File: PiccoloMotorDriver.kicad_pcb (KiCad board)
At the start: 6 copper layers, 60 x 60 mm, 114 parts, among them J10 AUX2, J11 C189893, J12 C265111, J2 01x03_MotorTerminal, J3 C189893, J4 C225127, J5 Screw_Terminal_01x02_POWER, J6 Connector, USB-TYPE-C-16P, J7 C225127, J8 AUX0, J9 AUX1, Q1 NE006NG, Q2 NE006NG, Q3 NE006NG, Q4 NE006NG, Q5 NE006NG, Q6 NE006NG, U1 SP485EEN, U2 XC6210B332MR, U3 XL1509, U4 TJA1050T/CM,118, U5 AS5047D, U6 USBLC6-2SC6, X2 X322516MLB4SI

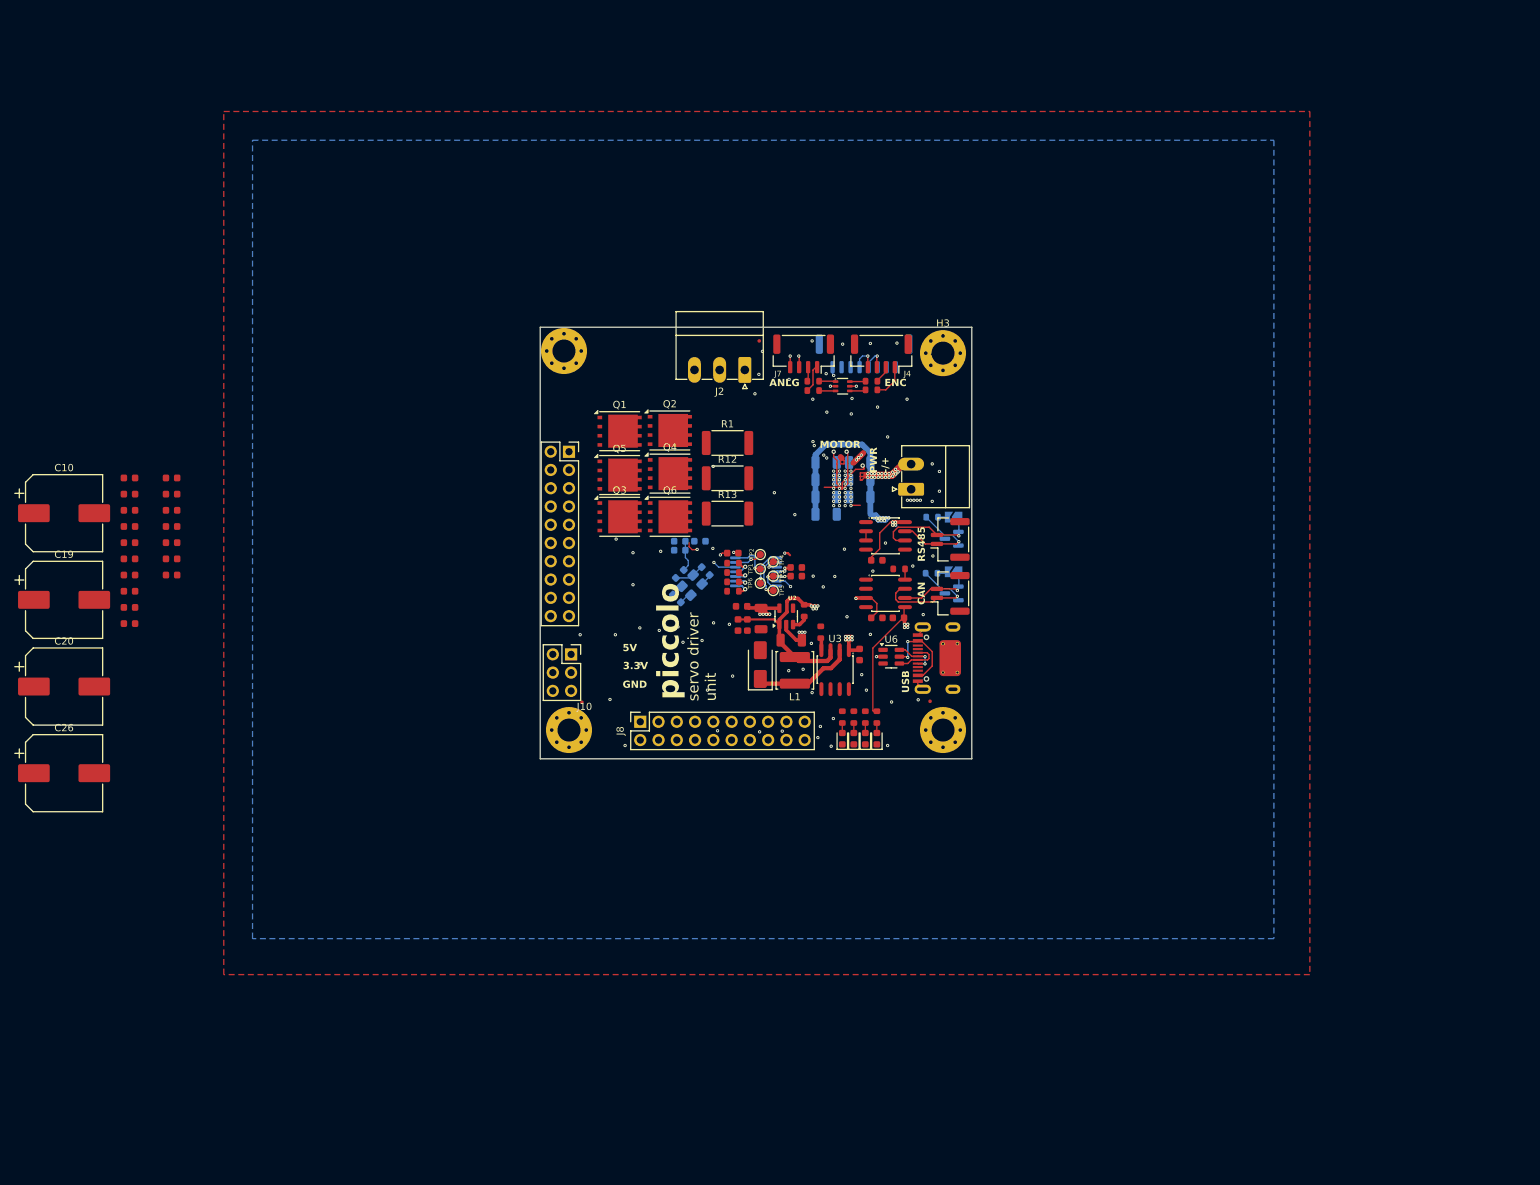
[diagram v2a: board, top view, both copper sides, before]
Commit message: Circular pcb edge cut
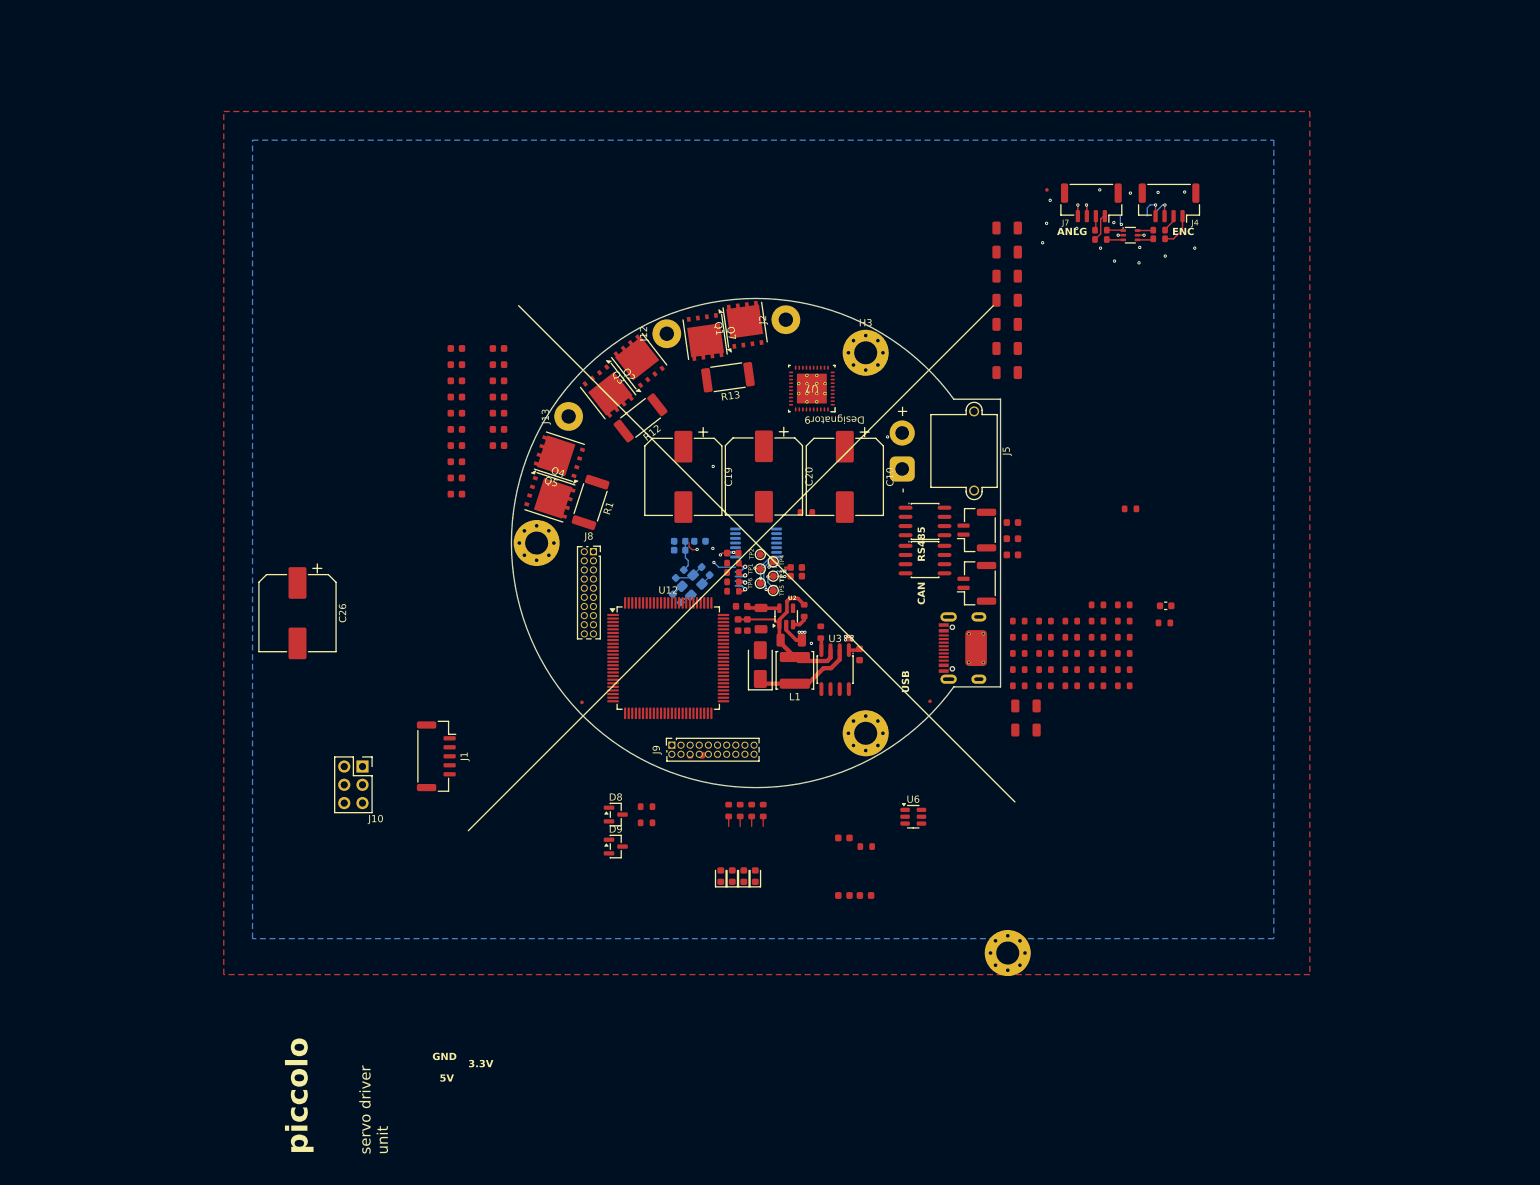
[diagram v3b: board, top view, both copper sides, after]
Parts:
- removed JP1, JP2: 120R Load, Jumper:SolderJumper-2_P1.3mm_Open_TrianglePad1.0x1.5mm
- removed Q6: NE006NG, Package_DFN_QFN:AO_DFN-8-1EP_5.55x5.2mm_P1.27mm_EP4.12x4.6mm
- added C39: 10uF, PCM_JLCPCB:C_1206, F.Cu at (175.5, 118.7)
- added C47: 100nF, PCM_JLCPCB:C_0603, F.Cu at (173.7, 93.2)
- added C48: 100nF, PCM_JLCPCB:C_0603, F.Cu at (173.7, 95.4)
- added C49: 100nF, PCM_JLCPCB:C_0603, F.Cu at (173.7, 97.7)
- added C53: 10uF, PCM_JLCPCB:C_1206, F.Cu at (175.5, 122.0)
- added FB2: ~, PCM_JLCPCB:FB_0603, F.Cu at (195.0, 104.7)
- added J1: Conn_01x06_SWD, Connector_JST:JST_GH_SM05B-GHS-TB_1x05-1MP_P1.25mm_Horizontal, F.Cu at (93.5, 125.7)
- added J13: Conn_01x01, Connector_Wire:SolderWire-2.5sqmm_1x01_D2.4mm_OD3.6mm, F.Cu at (112.0, 78.4)
- added Q7: NE006NG, Package_DFN_QFN:AO_DFN-8-1EP_5.55x5.2mm_P1.27mm_EP4.12x4.6mm, F.Cu at (130.9, 67.4)
- added R10: 22Ω, PCM_JLCPCB:R_0603, F.Cu at (174.5, 113.6)
- added R11: 22Ω, PCM_JLCPCB:R_0603, F.Cu at (174.5, 115.8)
- added R14: 10kΩ, PCM_JLCPCB:R_0603, F.Cu at (190.1, 91.2)
- added R15: 22Ω, PCM_JLCPCB:R_0603, F.Cu at (178.2, 106.8)
- added R16: 22Ω, PCM_JLCPCB:R_0603, F.Cu at (178.2, 109.1)
- added R17: 22Ω, PCM_JLCPCB:R_0603, F.Cu at (178.2, 111.3)
- added R18: 22Ω, PCM_JLCPCB:R_0603, F.Cu at (178.2, 113.6)
- added R19: 22Ω, PCM_JLCPCB:R_0603, F.Cu at (178.2, 115.8)
- added R2: 22Ω, PCM_JLCPCB:R_0603, F.Cu at (145.0, 91.8)
- added R20: 22Ω, PCM_JLCPCB:R_0603, F.Cu at (129.7, 125.5)
- added R23: 22Ω, PCM_JLCPCB:R_0603, F.Cu at (181.8, 106.8)
- added R25: 47kΩ, PCM_JLCPCB:R_0603, F.Cu at (181.8, 109.1)
- added R26: 22Ω, PCM_JLCPCB:R_0603, F.Cu at (194.8, 107.1)
- added R31: 22Ω, PCM_JLCPCB:R_0603, F.Cu at (181.8, 111.3)
- added R32: 22Ω, PCM_JLCPCB:R_0603, F.Cu at (181.8, 113.6)
- added R34: 1kΩ, PCM_JLCPCB:R_0603, F.Cu at (181.8, 115.8)
- added R40: 47kΩ, PCM_JLCPCB:R_0603, F.Cu at (185.5, 104.6)
- added R41: 1kΩ, PCM_JLCPCB:R_0603, F.Cu at (185.5, 106.8)
- added R42: 47kΩ, PCM_JLCPCB:R_0603, F.Cu at (185.5, 109.1)
- added R43: 1kΩ, PCM_JLCPCB:R_0603, F.Cu at (185.5, 111.3)
- added R5: 22Ω, PCM_JLCPCB:R_0603, F.Cu at (174.5, 106.8)
- added R58: 22Ω, PCM_JLCPCB:R_0603, F.Cu at (185.5, 113.6)
- added R59: 22Ω, PCM_JLCPCB:R_0603, F.Cu at (185.5, 115.8)
- added R60: 22Ω, PCM_JLCPCB:R_0603, F.Cu at (189.1, 104.6)
- added R61: 1kΩ, PCM_JLCPCB:R_0603, F.Cu at (189.1, 106.8)
- added R62: 1kΩ, PCM_JLCPCB:R_0603, F.Cu at (189.1, 109.1)
- added R63: 1kΩ, PCM_JLCPCB:R_0603, F.Cu at (189.1, 111.3)
- added R64: 47kΩ, PCM_JLCPCB:R_0603, F.Cu at (189.1, 113.6)
- added R65: 1kΩ, PCM_JLCPCB:R_0603, F.Cu at (189.1, 115.8)
- added R7: 22Ω, PCM_JLCPCB:R_0603, F.Cu at (174.5, 109.1)
- added R9: 22Ω, PCM_JLCPCB:R_0603, F.Cu at (174.5, 111.3)
- added U12: STM32H723VGT6, Package_QFP:LQFP-100_14x14mm_P0.5mm, F.Cu at (125.8, 112.0)
- added U7: DRV8353SRTAR, footprints:RTA0040B, F.Cu at (145.8, 74.5)
- C40, C41, C42, C43, C44, C45, C7, D8, D9, R22, R8: moved to F.Cu
- J12: value C265111 -> Conn_01x01; footprint Connector_JST:JST_GH_SM08B-GHS-TB_1x08-1MP_P1.25mm_Horizontal -> Connector_Wire:SolderWire-2.5sqmm_1x01_D2.4mm_OD3.6mm; moved to F.Cu
- J2: value 01x03_MotorTerminal -> Conn_01x01; footprint Connector_Phoenix_MC:PhoenixContact_MC_1,5_3-G-3.5_1x03_P3.50mm_Horizontal -> Connector_Wire:SolderWire-2.5sqmm_1x01_D2.4mm_OD3.6mm
- J5: footprint Connector_Phoenix_MC:PhoenixContact_MC_1,5_2-G-3.5_1x02_P3.50mm_Horizontal -> Connector_AMASS:AMASS_XT30PW-M_1x02_P2.50mm_Horizontal
- J8, J9: footprint Connector_PinSocket_2.54mm:PinSocket_2x10_P2.54mm_Vertical -> Connector_PinSocket_1.27mm:PinSocket_2x10_P1.27mm_Vertical
- moved C10 108.7 mm to (150.3, 86.8), turned to -90 degrees
- moved C20 101.6 mm to (139.1, 86.8), turned to -90 degrees
- moved C19 87.8 mm to (127.9, 86.8), turned to -90 degrees
- moved D8 60.4 mm to (118.5, 133.8), turned to 0 degrees
- moved D9 58.5 mm to (118.5, 138.2), turned to 0 degrees
- moved R8 56.5 mm to (122.8, 132.7), turned to 0 degrees
- moved R22 52.7 mm to (122.8, 134.9), turned to 0 degrees
- moved C1 48.9 mm to (102.2, 69.0)
- moved C11 48.9 mm to (96.3, 73.5)
- moved C12 48.9 mm to (96.3, 75.7)
- moved C16 48.9 mm to (96.3, 78.0)
- moved C17 48.9 mm to (96.3, 80.2)
- moved C2 48.9 mm to (102.2, 71.2)
- moved C27 48.9 mm to (96.3, 82.5)
- moved C28 48.9 mm to (102.2, 73.5)
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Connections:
- J12 pad 1: NRST -> /Inverter/PHASE_B
- J2 pad 1: Net-(J2-Pin_1) -> /Inverter/PHASE_A
- Q1 pad 1: Net-(Q1-G) -> Net-(U7-SPA)
- Q1 pad 2: Net-(J2-Pin_1) -> Net-(U7-SPA)
- Q1 pad 3: Vdrive -> Net-(U7-SPA)
- Q1 pad 4: (no net) -> Net-(Q1-G)
- Q1 pad 5: (no net) -> /Inverter/PHASE_A
- Q2 pad 1: Net-(Q2-G) -> /Inverter/PHASE_B
- Q2 pad 2: Net-(Q2-S) -> /Inverter/PHASE_B
- Q2 pad 3: Net-(J2-Pin_1) -> /Inverter/PHASE_B
- Q2 pad 4: (no net) -> Net-(Q2-G)
- Q2 pad 5: (no net) -> Vdrive
- Q3 pad 1: Net-(Q3-G) -> Net-(U7-SPB)
- Q3 pad 2: Net-(J2-Pin_2) -> Net-(U7-SPB)
- Q3 pad 3: Vdrive -> Net-(U7-SPB)
- Q3 pad 4: (no net) -> Net-(Q3-G)
- Q3 pad 5: (no net) -> /Inverter/PHASE_B
- Q4 pad 1: Net-(Q4-G) -> /Inverter/PHASE_C
- Q4 pad 2: Net-(Q4-S) -> /Inverter/PHASE_C
- Q4 pad 3: Net-(J2-Pin_2) -> /Inverter/PHASE_C
- Q4 pad 4: (no net) -> Net-(Q4-G)
- Q4 pad 5: (no net) -> Vdrive
- Q5 pad 1: Net-(Q5-G) -> Net-(U7-SPC)
- Q5 pad 2: Net-(J2-Pin_3) -> Net-(U7-SPC)
- Q5 pad 3: Vdrive -> Net-(U7-SPC)
- Q5 pad 4: (no net) -> Net-(Q5-G)
- Q5 pad 5: (no net) -> /Inverter/PHASE_C
- R1 pad 1: Net-(Q6-S) -> Net-(U7-SPC)
- R12 pad 1: Net-(Q4-S) -> Net-(U7-SPB)
- R13 pad 1: Net-(Q2-S) -> Net-(U7-SPA)
- R22 pad 1: Net-(JP2-B) -> /IO/can_termination_B
- R8 pad 1: Net-(JP1-B) -> /IO/rs485_termination_B
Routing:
- net Vdrive: track 99.8 -> 4.26 mm, vias 33 -> 5
- net +5V: track 109.3 -> 27.5 mm, vias 12 -> 1
- net +3.3V: track 89.6 -> 15.3 mm, vias 11 -> 3
- net /IO/CAN+: track 17.8 -> 0.00 mm, vias 1 -> 0
- net /IO/RS485+: track 15.1 -> 0.00 mm, vias 1 -> 0
- net /IO/RS485-: track 14.9 -> 0.00 mm, vias 1 -> 0
- net Net-(U6-VBUS): track 12.0 -> 0.00 mm, vias 2 -> 0
- net GND: track 50.9 -> 39.0 mm, vias 126 -> 27
- net /IO/CAN-: track 10.6 -> 0.00 mm, vias 1 -> 0
- net (no net): track 15.8 -> 8.10 mm, vias 7 -> 0
- net Net-(J6-D+-PadA6): track 6.61 -> 0.00 mm
- net Net-(J6-D--PadA7): track 5.98 -> 0.00 mm, vias 2 -> 0
- net Net-(U5-A): track 5.29 -> 0.79 mm
- net Net-(U5-B): track 3.92 -> 0.00 mm, vias 1 -> 0
- net /Mcu/PB10: track 0.00 -> 2.54 mm
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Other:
- board size 60 x 60 mm -> 68 x 68 mm
- board text removed: "CAN Termination"
- board text removed: "MOTOR"
- board text removed: "PWR -/+"
- board text removed: "RS485 Termination"

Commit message: Rough placement
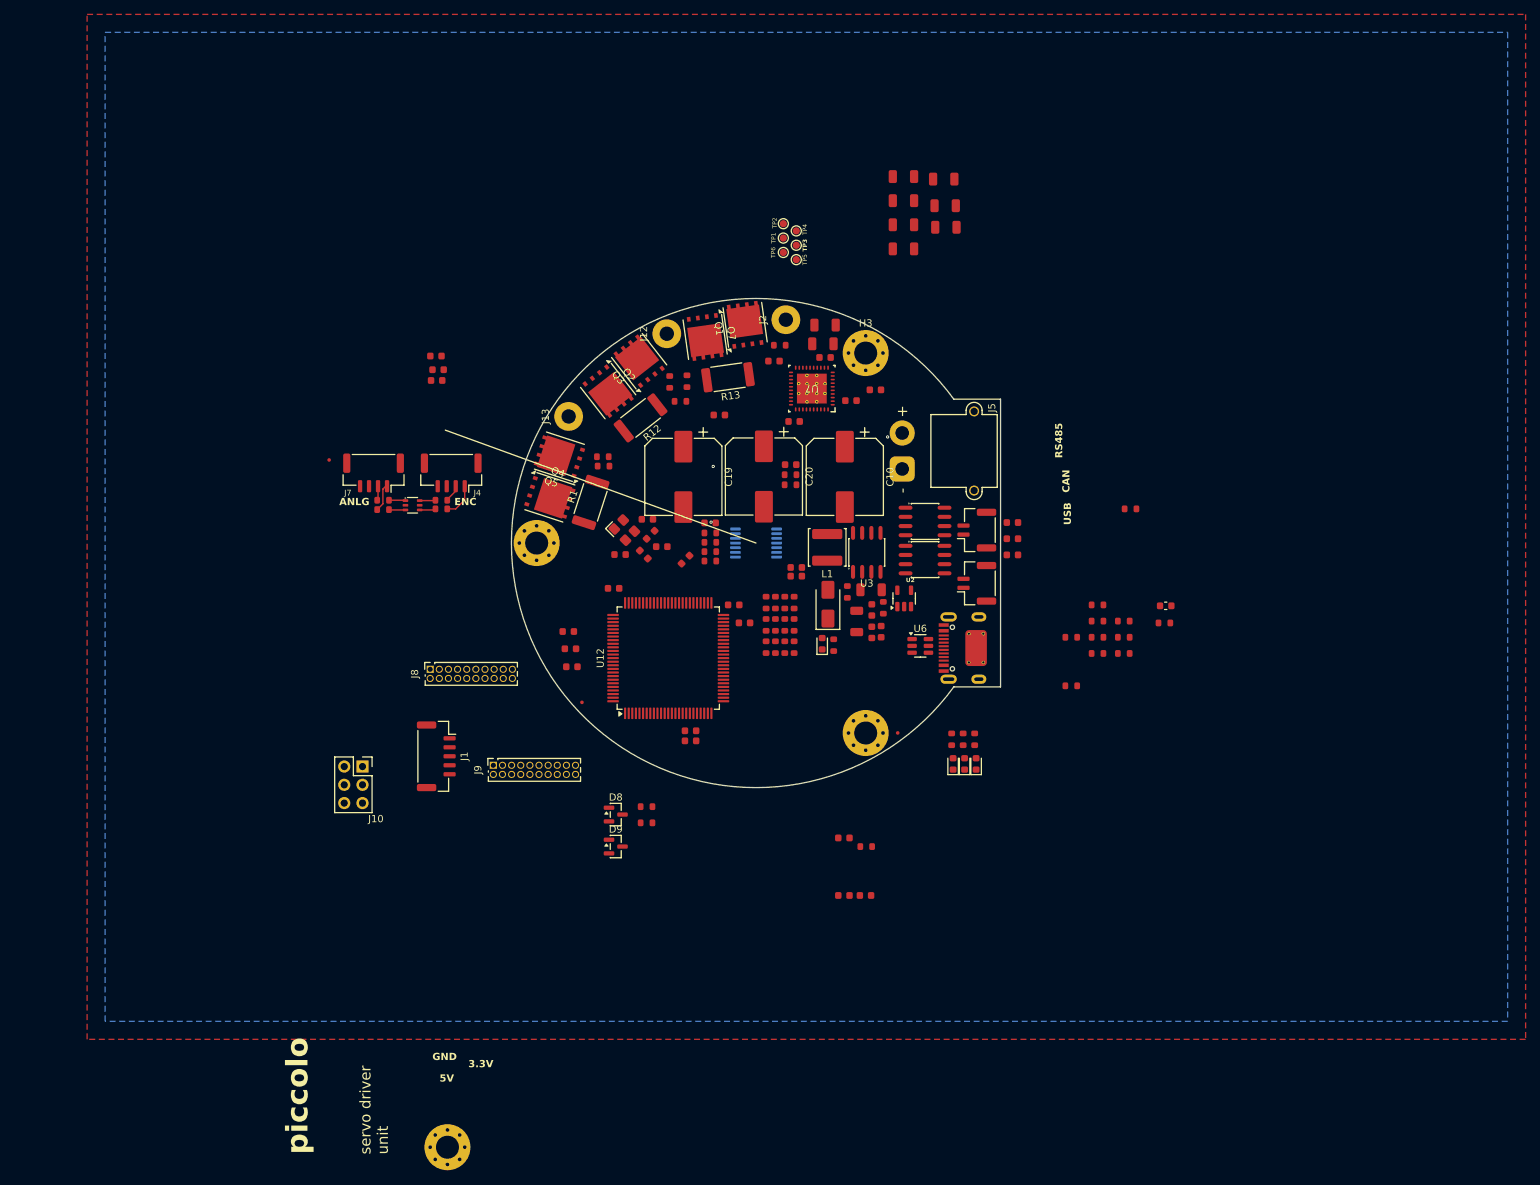
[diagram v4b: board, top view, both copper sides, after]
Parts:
- removed C26: 100uF / 100V, Capacitor_SMD:CP_Elec_10x10.5
- C30, C31, C32, C33, C8, C9, X2: moved to F.Cu
- moved D1 106.6 mm to (90.3, 90.7)
- moved J4 106.6 mm to (95.6, 86.2)
- moved R30 106.6 mm to (94.3, 90.0)
- moved R35 106.6 mm to (94.3, 91.2)
- moved FID3 106.6 mm to (78.7, 84.4)
- moved J7 106.6 mm to (84.8, 86.2)
- moved R33 106.6 mm to (86.2, 91.3)
- moved R36 106.6 mm to (86.2, 90.0)
- moved H1 82.4 mm to (95.1, 180.0)
- moved R11 66.0 mm to (116.7, 84.0)
- moved R10 64.3 mm to (116.8, 85.3), turned to 180 degrees
- moved R9 61.5 mm to (126.0, 73.6), turned to 90 degrees
- moved C53 60.7 mm to (147.3, 68.3)
- moved C39 59.9 mm to (147.6, 65.7)
- moved C17 58.5 mm to (154.6, 74.7)
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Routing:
- net GND: track 39.0 -> 5.08 mm, vias 27 -> 3
- net +5V: track 27.5 -> 0.00 mm, vias 1 -> 0
- net NRST: track 20.7 -> 0.00 mm, vias 3 -> 0
- net +3.3V: track 15.3 -> 0.00 mm, vias 3 -> 0
- net Net-(U3-OUTPUT): track 14.0 -> 0.00 mm
- net (no net): track 8.10 -> 0.00 mm
- net Net-(U5-V): track 6.29 -> 0.00 mm, vias 1 -> 0
- net Net-(U5-W/PWM): track 5.18 -> 0.00 mm, vias 1 -> 0
- net Vdrive: track 4.26 -> 0.00 mm, vias 5 -> 0
- net Net-(U5-I/PWM): track 2.98 -> 0.00 mm, vias 1 -> 0
- net Net-(U5-MOSI): track 2.74 -> 0.00 mm, vias 1 -> 0
- net Net-(U5-~{CS}): track 2.55 -> 0.00 mm, vias 1 -> 0
- net /Mcu/PB10: track 2.54 -> 0.00 mm
- net Net-(U5-MISO): track 2.47 -> 0.00 mm, vias 1 -> 0
- net Net-(U5-CLK): track 2.37 -> 0.00 mm, vias 1 -> 0
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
